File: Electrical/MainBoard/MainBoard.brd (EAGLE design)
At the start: 120 x 100 mm, 121 parts, among them IC1 MEGA16-P, IC2 MCP4922-E/SL, IC3 MCP4921-E/SN, IC4 TL074D, IC5 TL074D, IC6 FT232RL, Q1 BC140-10, Q2 BC160, Q3 BC140-10, Q4 BC160, Q5 BD239, Q6 BD240, Q7 BC557, Q8 16MHz, X1 FH12-45S-0.5SH, X2 22-23-2021, X3 PN61729-S

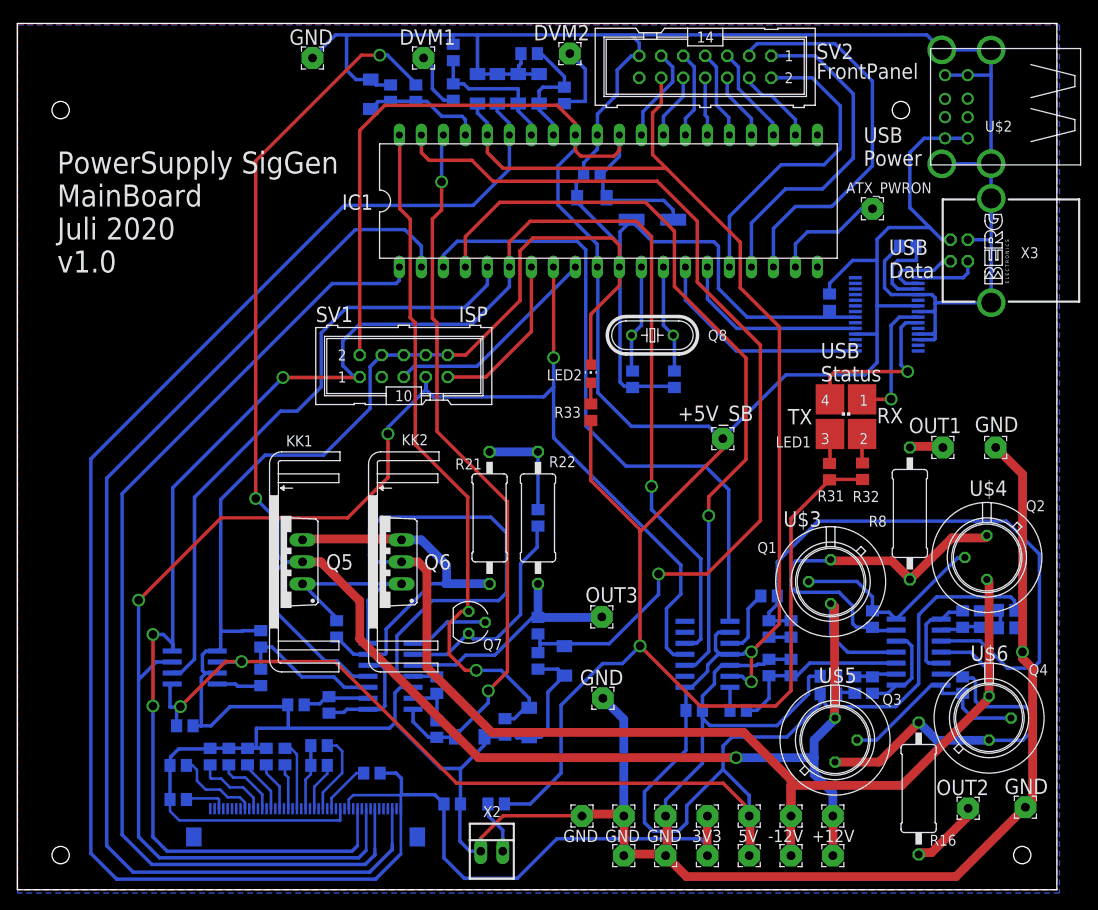
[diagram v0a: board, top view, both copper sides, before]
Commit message: Board resized
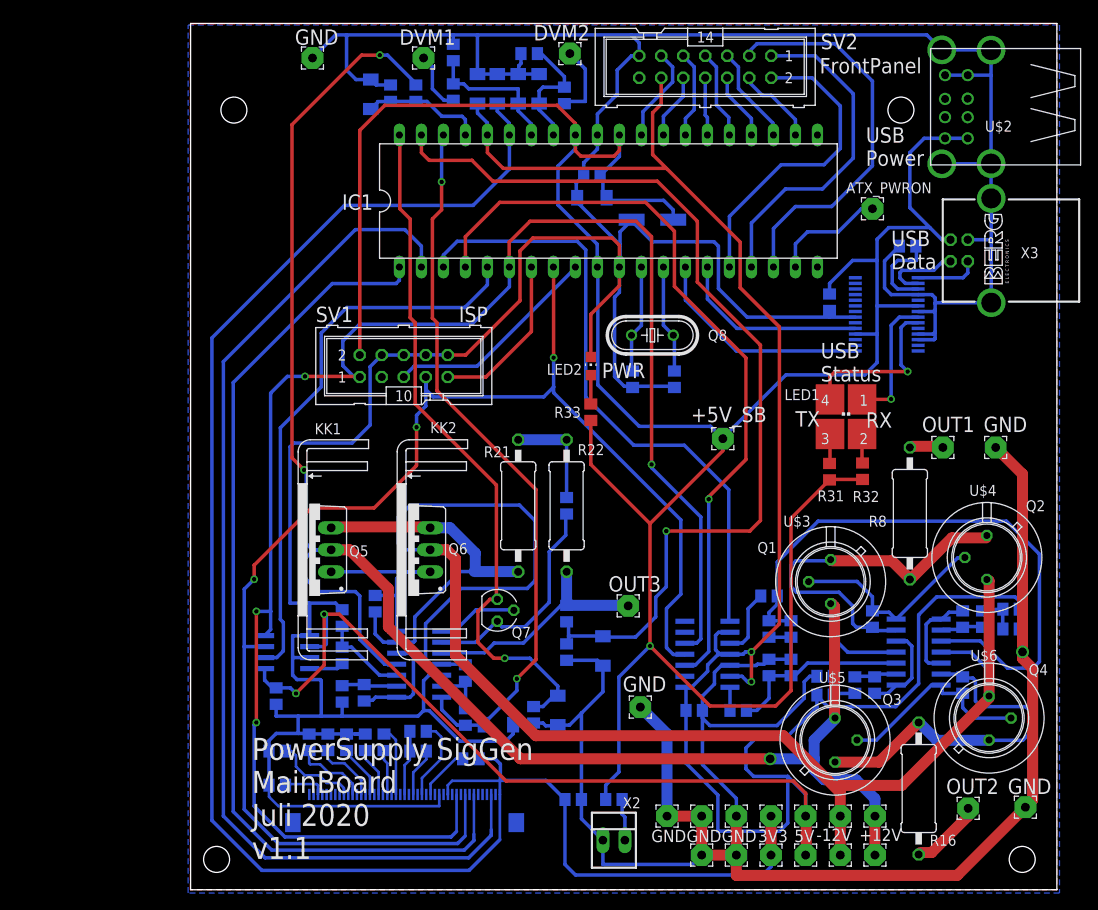
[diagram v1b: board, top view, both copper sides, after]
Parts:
- moved X2 14.2 mm to (78.9, 5.71)
- moved C12 14.0 mm to (74.2, 10.4)
- moved R34 13.6 mm to (78.9, 10.4), turned to 180 degrees
- moved C21 11.5 mm to (40.0, 16.0)
- moved C22 11.5 mm to (40.0, 12.1)
- moved C13 11.5 mm to (62.4, 15.1)
- moved C14 11.5 mm to (56.3, 18.3)
- moved C15 11.5 mm to (56.3, 16.0)
- moved C16 11.5 mm to (52.3, 17.0)
- moved C17 11.5 mm to (50.2, 17.0)
- moved C18 11.5 mm to (48.0, 17.0)
- moved C19 11.5 mm to (45.8, 17.0)
- moved C20 11.5 mm to (43.7, 17.0)
- moved X1 11.5 mm to (52.7, 7.75)
- moved C4 11.1 mm to (39.9, 22.4), turned to 90 degrees
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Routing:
- net GND: track 699.3 -> 682.9 mm
- net +3V3: track 223.8 -> 208.5 mm
- net SCK: track 182.7 -> 167.7 mm
- net VCC: track 329.7 -> 319.3 mm
- net LCD_CS: track 133.8 -> 123.5 mm
- net LCD_A0: track 119.5 -> 110.5 mm
- net MOSI: track 202.9 -> 194.3 mm
- net N$16: track 16.9 -> 10.0 mm
- net PS_CS: track 71.6 -> 64.8 mm
- net +5V: track 300.9 -> 306.5 mm
- net -12V: track 179.3 -> 175.6 mm
- net N$20: track 26.9 -> 24.2 mm
- net DDS_LDAC: track 74.0 -> 72.1 mm
- net N$17: track 7.99 -> 6.39 mm
- net BL_A: track 6.19 -> 4.83 mm
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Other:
- board size 120 x 100 mm -> 100 x 100 mm
- board text added: "PWR"
- board text added: "PowerSupply SigGen MainBoard Juli 2020 v1.1"
- board text removed: "PowerSupply SigGen MainBoard Juli 2020 v1.0"

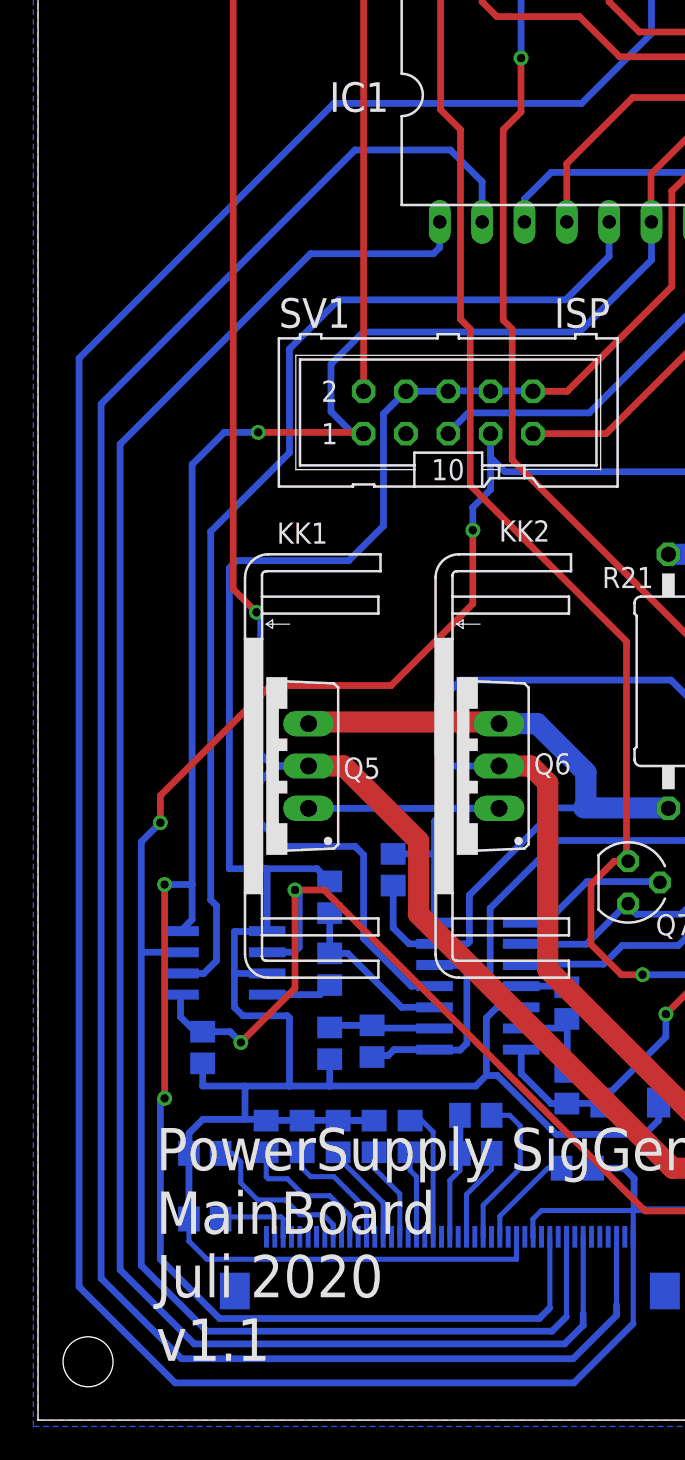
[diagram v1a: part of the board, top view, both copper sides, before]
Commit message: Resistors add to MainBoard to convert 5V to 3.3V for LCD signals
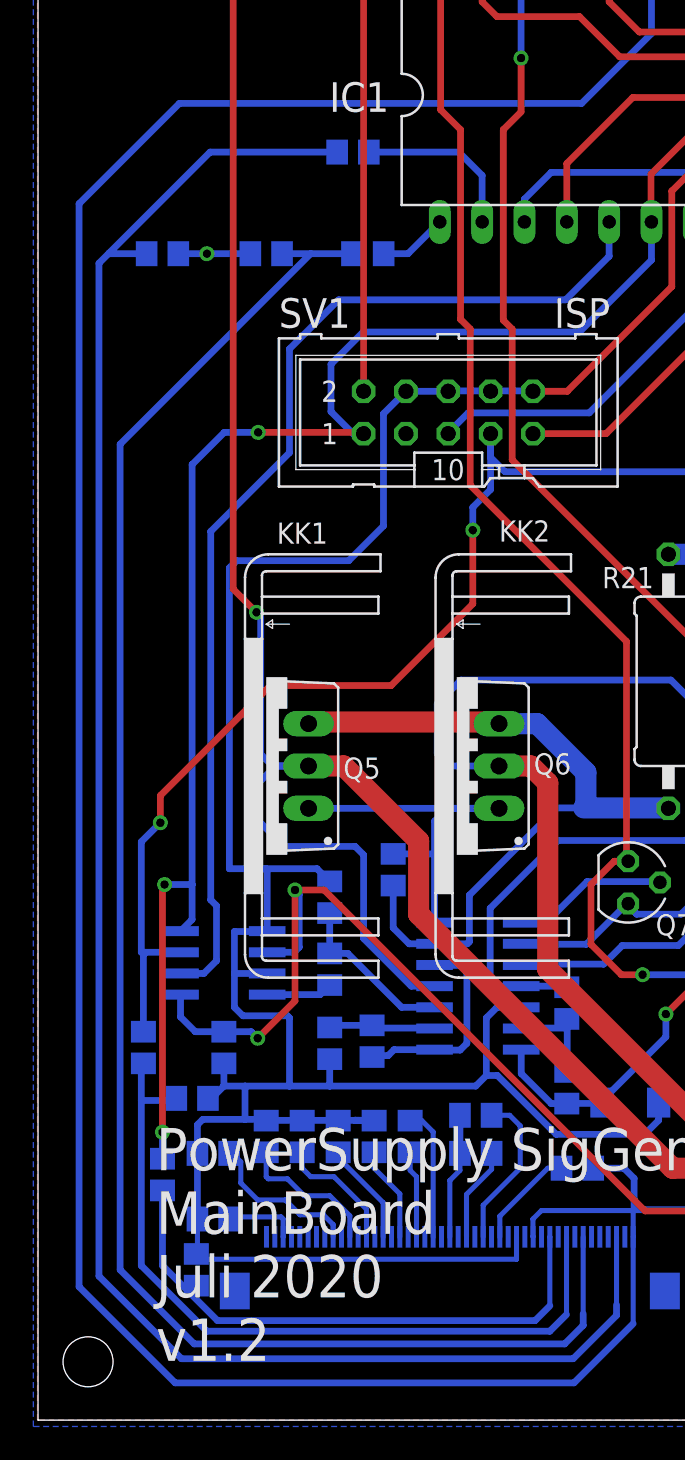
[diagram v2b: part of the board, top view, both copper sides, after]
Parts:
- added R39, R40, R41, R42: 1k, OwnDevices:R0805
- added R43, R44, R45, R46: 2k4, OwnDevices:R0805
- moved C4 1.27 mm to (41.1, 22.4)
- moved C21 0.51 mm to (40.5, 16.0)
- moved C22 0.51 mm to (40.5, 12.1)
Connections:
- net DDS_CS renamed !DDS_CS
- net DDS_LDAC renamed !DDS_LDAC
- net PS_CS renamed !PS_CS
- removed net LCD_CS: IC1.2, X1.3
- new net !LCD_CS: IC1.2, R39.2
- new net !LCD_CS_3V3: R39.1, R43.1, X1.3
- new net LCD_A0_3V3: R40.1, R44.1, X1.7
- new net MOSI_3V3: R42.1, R46.1, X1.11
- new net SCK_3V3: R41.1, R45.1, X1.9
- net GND: now also R43.2, R44.2, R45.2, R46.2
- net LCD_A0: now also R40.2; no longer X1.7
- net MOSI: now also R42.2; no longer X1.11
- net SCK: now also R41.2; no longer X1.9
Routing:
- net LCD_CS: track 123.5 -> 0.00 mm
- net !LCD_CS_3V3: track 0.00 -> 119.0 mm
- net LCD_A0: track 110.5 -> 4.16 mm
- net LCD_A0_3V3: track 0.00 -> 105.3 mm
- net SCK_3V3: track 0.00 -> 46.6 mm
- net SCK: track 167.7 -> 121.4 mm
- net MOSI: track 194.3 -> 158.9 mm
- net MOSI_3V3: track 0.00 -> 34.2 mm
- net !LCD_CS: track 0.00 -> 10.2 mm
- net +3V3: track 208.5 -> 213.9 mm
- net GND: track 682.9 -> 687.1 mm, vias 1 -> 2
- net MV2: track 4.92 -> 4.41 mm
- net MV1: track 10.00 -> 9.49 mm
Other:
- board text added: "PowerSupply SigGen MainBoard Juli 2020 v1.2"
- board text removed: "PowerSupply SigGen MainBoard Juli 2020 v1.1"

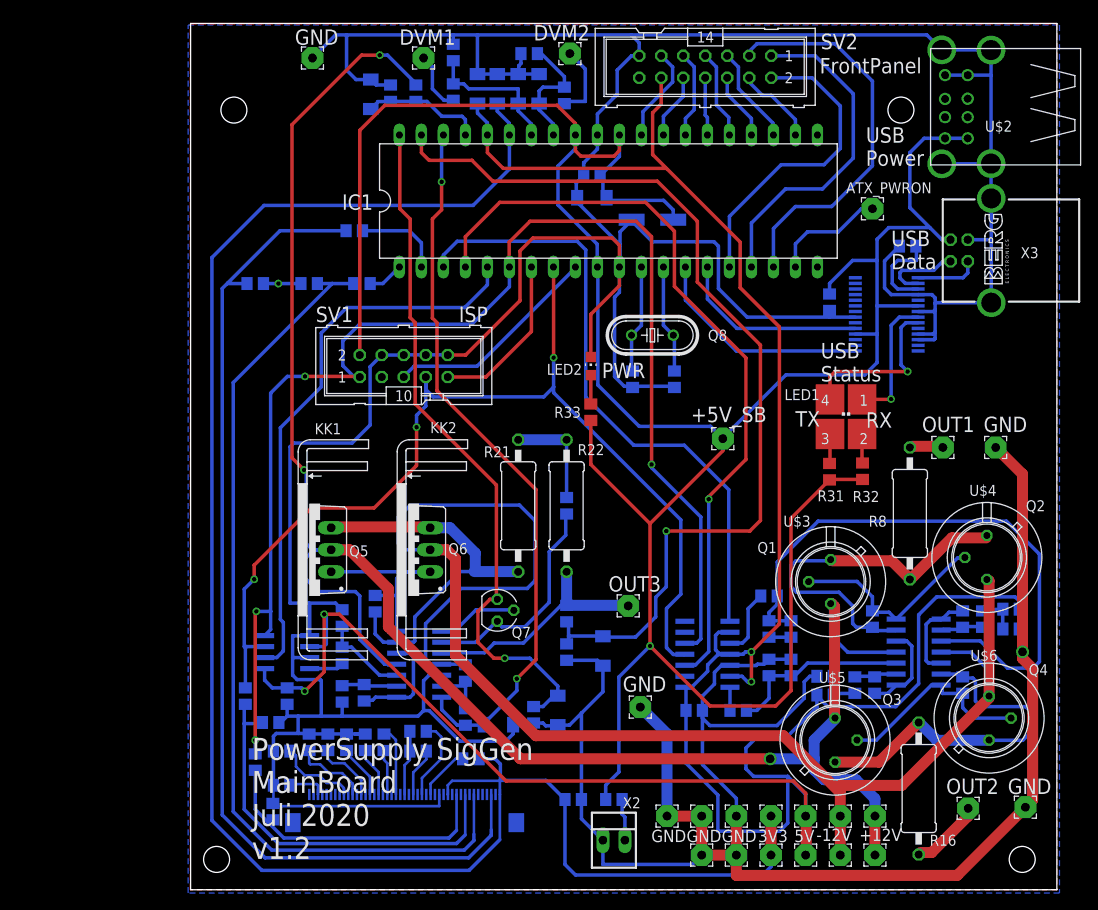
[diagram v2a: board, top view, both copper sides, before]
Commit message: Updated to new project name (PS_Fgen_HW), removed Z-Diode and ATX_PWR_ON signal from MainBoard
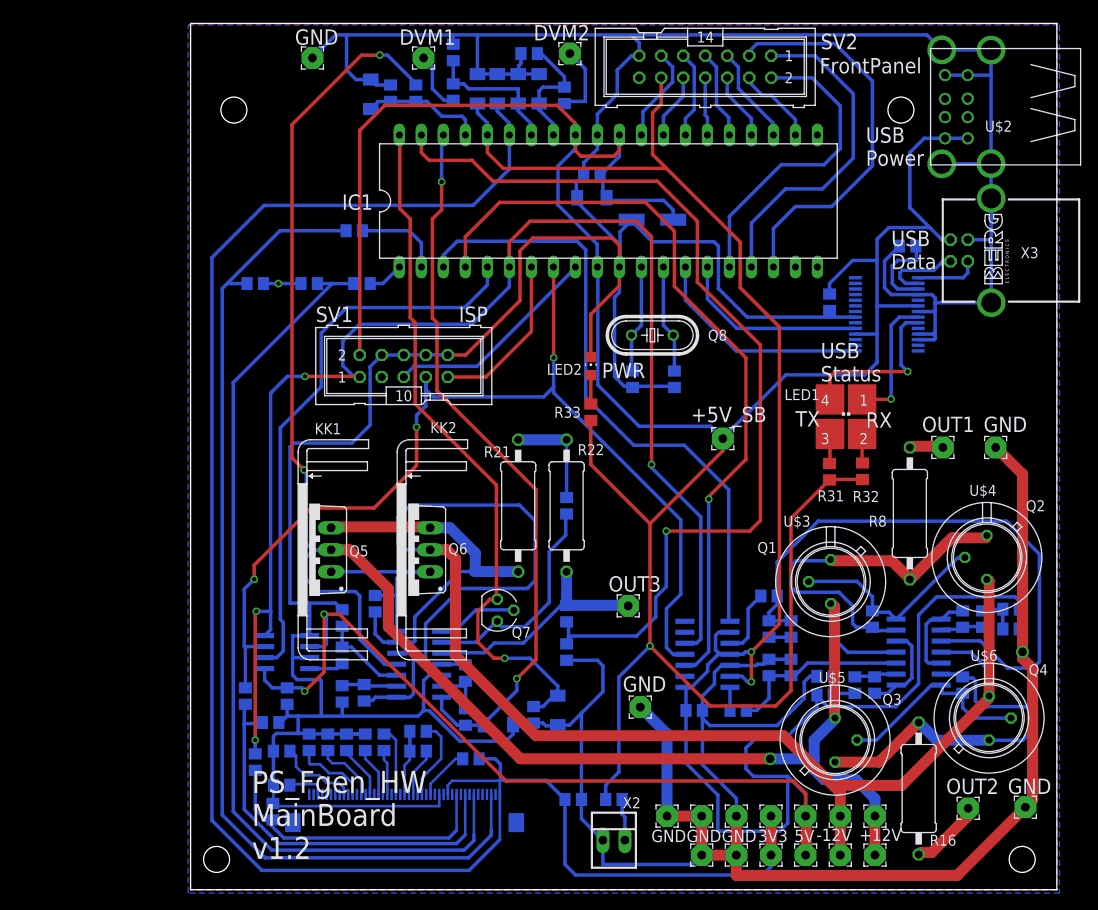
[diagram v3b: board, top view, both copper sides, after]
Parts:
- removed ATX_PWRON: (no value), OwnDevices:2,54/1,0
- removed D2: 5V, diode:SOD80C
- IC1: value MEGA16-P -> MEGA1284-P
- R43, R44, R45, R46: value 2k4 -> 2k
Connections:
- removed net ATX_PWR_ON: ATX_PWRON.1, IC1.19
- net GND: no longer D2.A
- net PS_VOLT: no longer D2.C
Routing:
- net ATX_PWR_ON: track 13.2 -> 0.00 mm
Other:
- board text added: "PS_Fgen_HW MainBoard v1.2"
- board text removed: "PowerSupply SigGen MainBoard Juli 2020 v1.2"

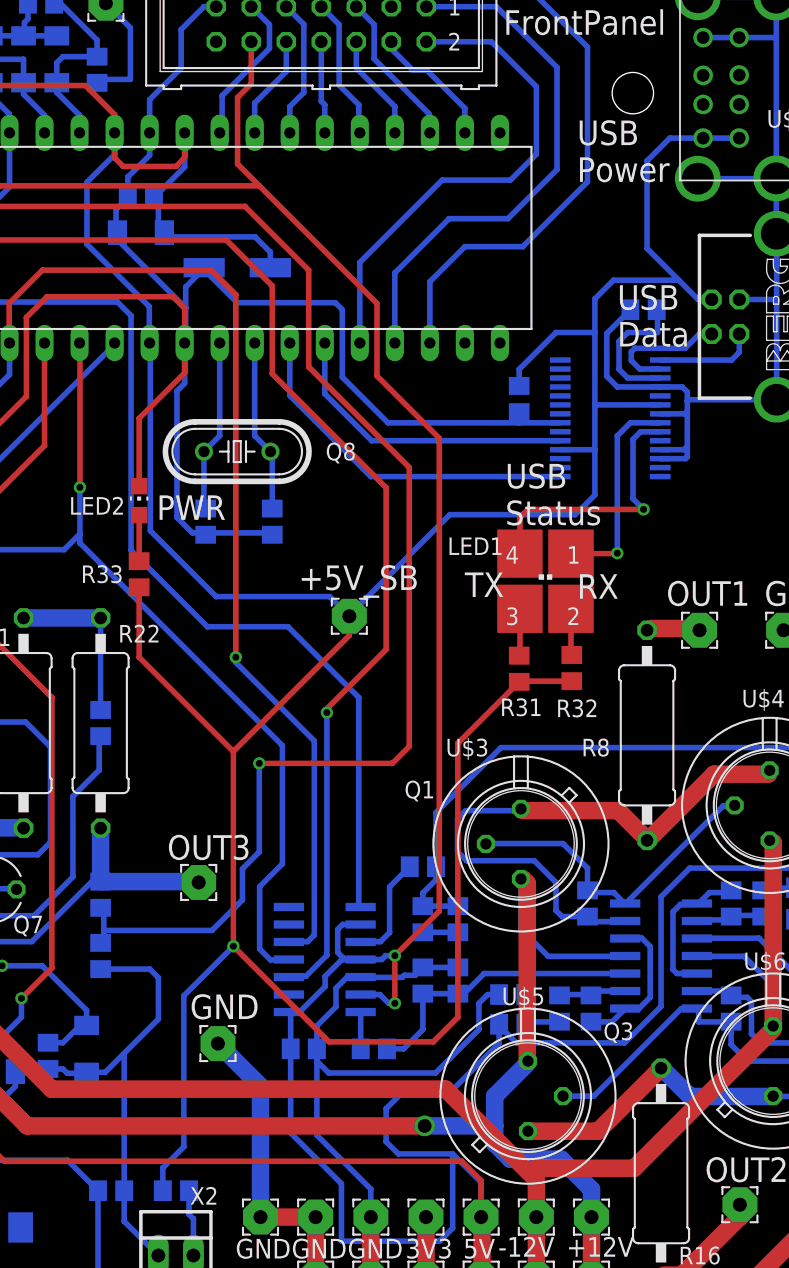
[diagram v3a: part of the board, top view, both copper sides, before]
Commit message: MainBoard: Removed ATX_5V_SB input (combined VCC and +5V nets)
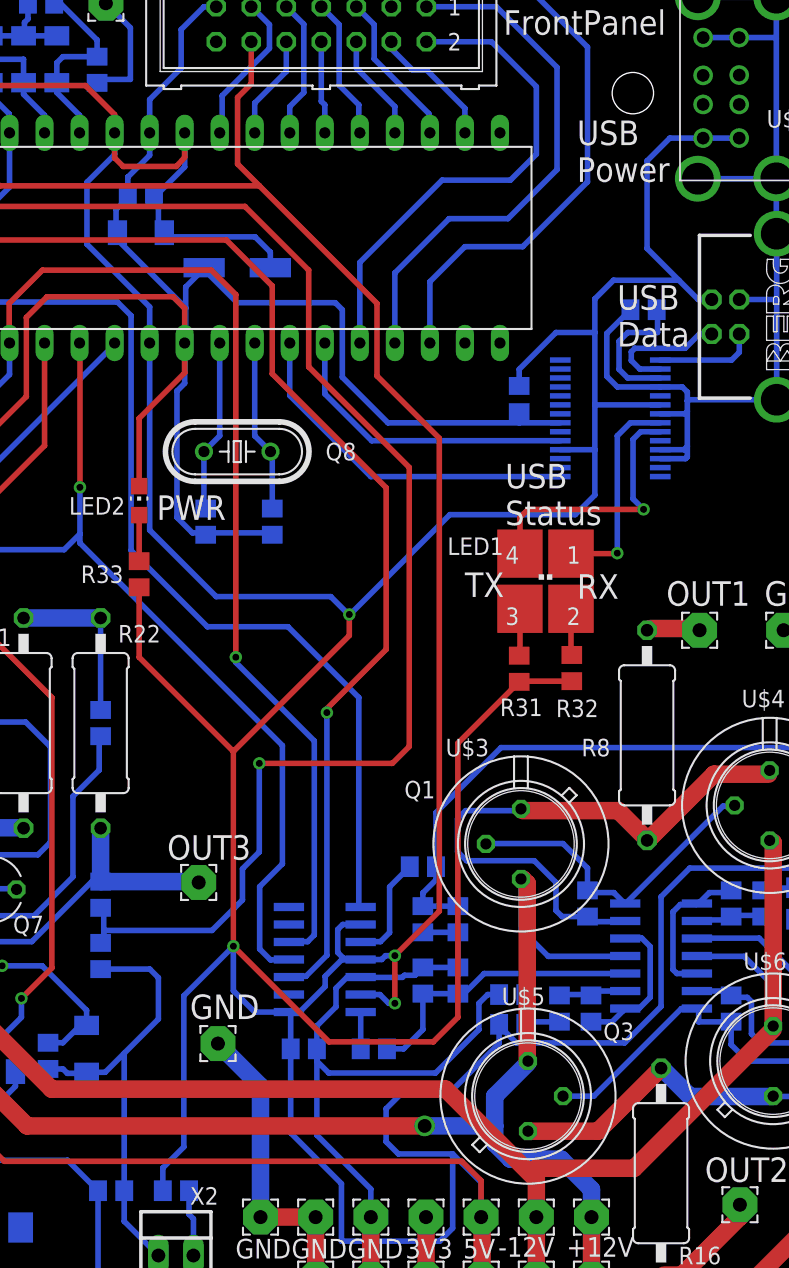
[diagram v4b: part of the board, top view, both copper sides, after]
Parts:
- removed ATX_+5V_SB: (no value), OwnDevices:2,54/1,0
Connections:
- removed net VCC: ATX_+5V_SB.1, C10.1, C8.2, C9.+, D7.C, IC1.10, IC1.30, IC1.32, IC6.20, IC6.4, R31.2, R32.2, R33.2, R34.1, SV1.2, U$2.P$10, U$2.P$12, X3.1
- net +5V: now also C10.1, C8.2, C9.+, D7.C, IC1.10, IC1.30, IC1.32, IC6.20, IC6.4, R31.2, R32.2, R33.2, R34.1, SV1.2, U$2.P$10, U$2.P$12, X3.1
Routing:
- net +5V: track 306.7 -> 634.1 mm, vias 4 -> 6
- net VCC: track 319.3 -> 0.00 mm, vias 1 -> 0
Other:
- board text removed: "+5V_SB"
